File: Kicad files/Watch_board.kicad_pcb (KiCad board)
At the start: 2 copper layers, 45.5 x 35 mm, 60 parts, among them J1 USB_C_Receptacle_USB2.0, J2 MOT1, J3 MOT2, Q1 BC846, SW2 BTN_L, SW3 BTN_R, U1 LTC3531, U2 MAX1811, U3 BMP280, U4 DS3231MZ, U5 STM32L031K6Tx, U6 xc9141

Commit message: updated PCB version
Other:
- board text added: "STM32Watch v1.1"
- board text removed: "STM32Watch v1.0"
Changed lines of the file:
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@@
     (effects (font (size 1 1) (thickness 0.15)) (justify mirror))
   )
-  (gr_text "STM32Watch v1.0" (at 92 61.75 90) (layer "F.SilkS")
+  (gr_text "STM32Watch v1.1" (at 92 61.75 90) (layer "F.SilkS")
     (effects (font (size 1 1) (thickness 0.15)))
   )

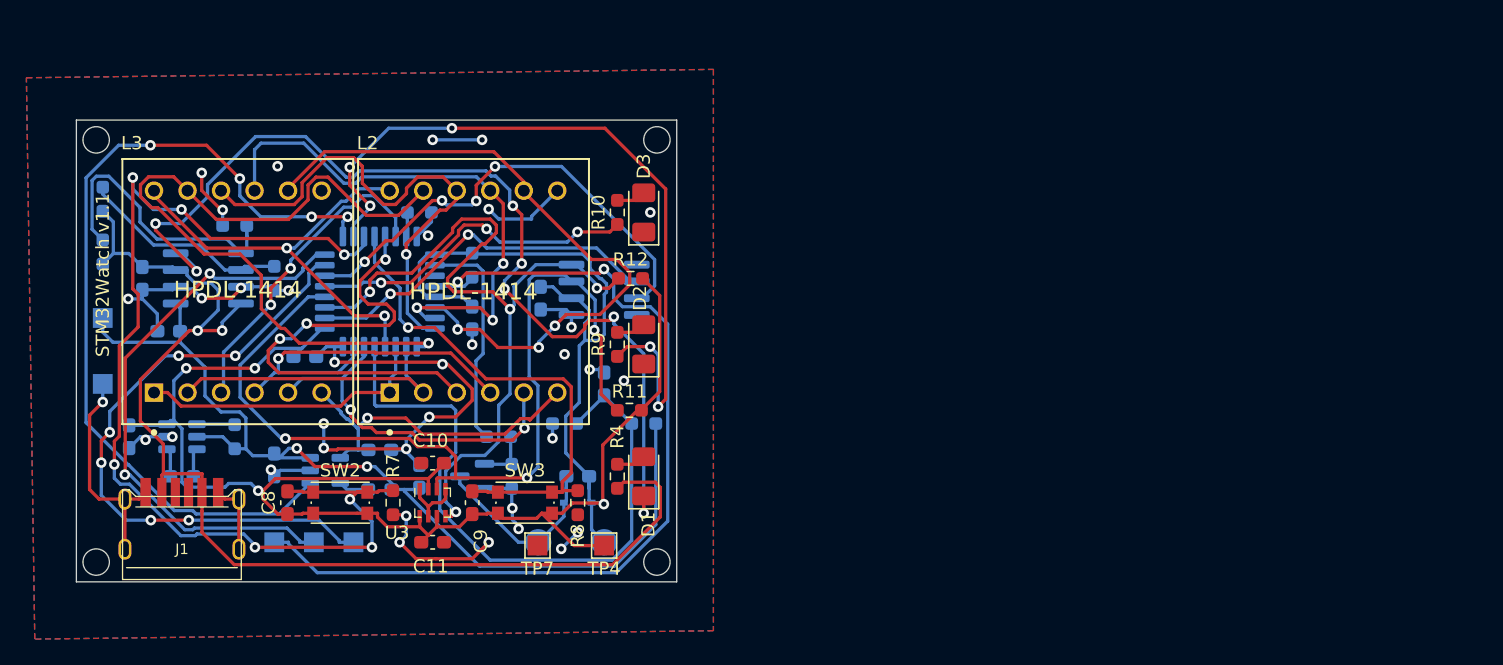
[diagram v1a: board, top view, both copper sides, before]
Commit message: updated to HCMS-2904 (WIP)
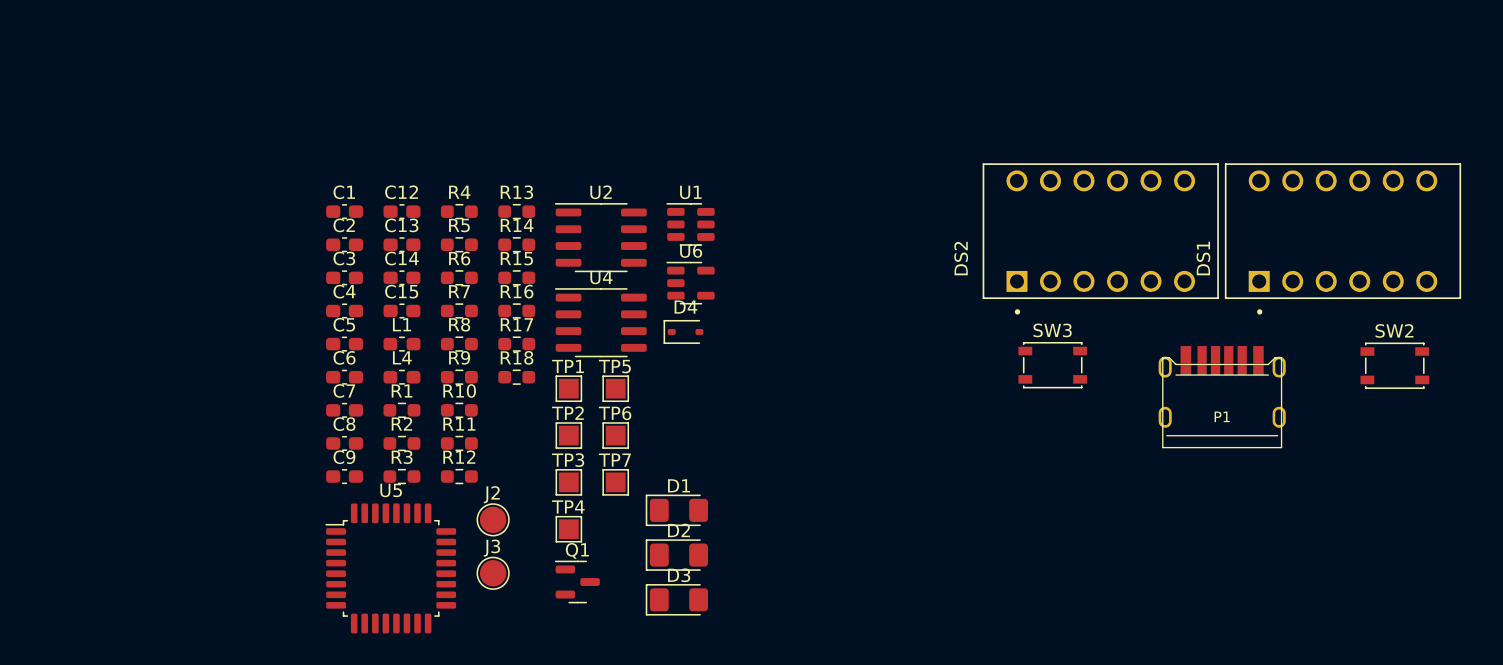
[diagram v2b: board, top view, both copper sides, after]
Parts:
- removed C10, C11: 0.1uF, Capacitor_SMD:C_0603_1608Metric_Pad1.08x0.95mm_HandSolder
- removed J1: USB_C_Receptacle_USB2.0, USB-C-Connectors:TYPE-C-31-M-17_handsolder
- removed L2, L3: HPDL-1414, eec:Broadcom-HPDL-1414-0
- removed U3: BMP280, Package_LGA:Bosch_LGA-8_2x2.5mm_P0.65mm_ClockwisePinNumbering
- added DS1: HCMS-2904, HCMS-290x:DIPS762W51P254L1778H508Q12, F.Cu at (186.0, 58.4)
- added DS2: HCMS-2904, HCMS-290x:DIPS762W51P254L1778H508Q12, F.Cu at (167.6, 58.4)
- added P1: USB_C_Plug_USB2.0, USB-C-Connectors:TYPE-C-31-M-17_handsolder, F.Cu at (176.8, 72.5)
- C1, C12, C13, C14, C15, C2, C3, C4, C5, C6, C7, D4, J2, J3, L1, L4, Q1, R1, R13, R14, R15, R16, R17, R18, R2, R3, R5, R6, TP1, TP2, TP3, TP5, TP6, U1, U2, U4, U5, U6: moved to F.Cu
- SW2, SW3: footprint Button_Switch_SMD:SW_Push_1P1T_NO_CK_KMR2 -> Button_Switch_SMD:SW_SPST_PTS810
- moved SW2 80.6 mm to (189.9, 68.6)
- moved U1 41.8 mm to (136.6, 57.9)
- moved SW3 41.3 mm to (164.0, 68.6)
- moved TP5 39.2 mm to (130.9, 70.4), turned to 0 degrees
- moved TP6 39.1 mm to (130.9, 73.9), turned to 0 degrees
- moved U6 31.1 mm to (136.6, 62.4)
- moved U2 29.9 mm to (129.8, 58.9), turned to 0 degrees
- moved D3 29.5 mm to (135.7, 86.4), turned to 0 degrees
- moved R6 27.7 mm to (119.0, 62.0), turned to 0 degrees
- moved R5 27.0 mm to (119.0, 59.5), turned to 0 degrees
- moved TP2 23.7 mm to (127.3, 73.9), turned to 0 degrees
- moved R4 23.4 mm to (119.0, 56.9), turned to 0 degrees
- moved R3 22.9 mm to (114.7, 77.0)
- moved C2 21.9 mm to (110.3, 59.5), turned to 0 degrees
- moved U5 21.0 mm to (113.9, 84.0), turned to 0 degrees
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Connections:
- U5 pad 21: LED_R -> unconnected-(U5-PA11-Pad21)
- U5 pad 26: LED_G -> unconnected-(U5-PB3-Pad26)
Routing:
- net 3V3: track 158.0 -> 0.00 mm, vias 4 -> 0
- net GND: track 127.3 -> 0.00 mm, vias 35 -> 0
- net VUSB: track 87.9 -> 0.00 mm, vias 2 -> 0
- net BTN_L: track 81.0 -> 0.00 mm, vias 7 -> 0
- net Net-(D1-K): track 75.5 -> 0.00 mm, vias 7 -> 0
- net BAT+: track 74.0 -> 0.00 mm, vias 2 -> 0
- net NRST: track 69.9 -> 0.00 mm, vias 2 -> 0
- net SDA: track 69.2 -> 0.00 mm, vias 3 -> 0
- net DISP_EN: track 64.9 -> 0.00 mm, vias 4 -> 0
- net SCL: track 59.7 -> 0.00 mm, vias 4 -> 0
- net LED_G: track 57.8 -> 0.00 mm, vias 5 -> 0
- net D3: track 56.8 -> 0.00 mm, vias 1 -> 0
- net D0: track 51.0 -> 0.00 mm, vias 3 -> 0
- net ADC: track 50.3 -> 0.00 mm
- net Net-(U5-PA13): track 48.7 -> 0.00 mm, vias 6 -> 0
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- removed copper zone on B.Cu, net GND
- removed copper zone on F.Cu, net GND
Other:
- board outline removed
- board text removed: "BAT+"
- board text removed: "BAT-"
- board text removed: "MOT1"
- board text removed: "MOT2"
- board text removed: "RES"
- board text removed: "STM32Watch v1.1"
- board text removed: "TCK"
- board text removed: "TMS"

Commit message: updated kicad schematics to add light sensor, updated code
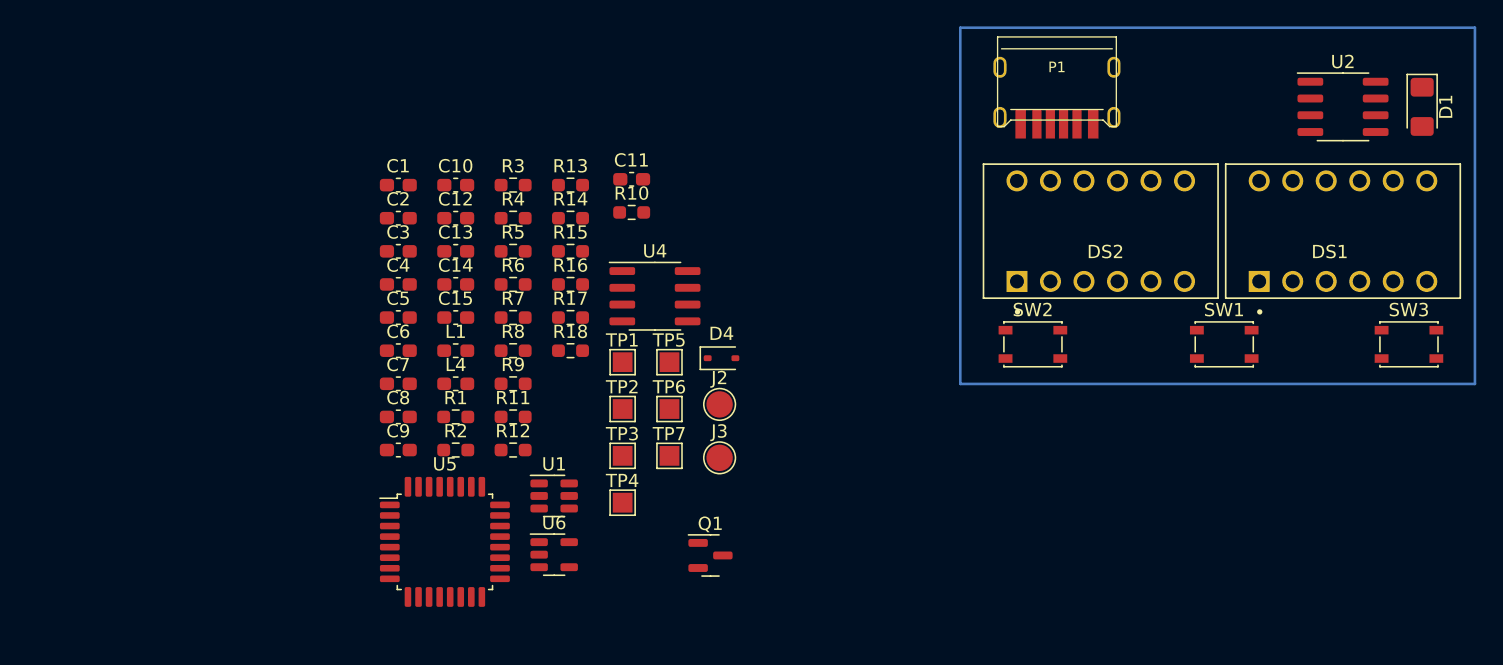
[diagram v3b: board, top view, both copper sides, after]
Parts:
- removed D2: LED_G, LED_SMD:LED_1206_3216Metric_Pad1.42x1.75mm_HandSolder
- removed D3: LED_R, LED_SMD:LED_1206_3216Metric_Pad1.42x1.75mm_HandSolder
- added C10: 0.1uF, Capacitor_SMD:C_0603_1608Metric_Pad1.08x0.95mm_HandSolder, F.Cu at (118.8, 54.9)
- added C11: 0.1uF, Capacitor_SMD:C_0603_1608Metric_Pad1.08x0.95mm_HandSolder, F.Cu at (132.1, 54.5)
- added SW1: BTN_M, Button_Switch_SMD:SW_SPST_PTS810, F.Cu at (177.0, 67.0)
- R10: value 4.7k -> 1k
- R9: value 22k -> 10k
- moved D1 64.1 mm to (192.0, 49.0), turned to -90 degrees
- moved U2 57.1 mm to (186.0, 49.0)
- moved P1 29.3 mm to (164.3, 46.0), turned to 180 degrees
- moved SW2 27.5 mm to (162.5, 67.0)
- moved SW3 27.0 mm to (191.0, 67.0)
- moved R3 23.6 mm to (123.1, 54.9)
- moved U1 23.0 mm to (126.2, 78.5)
- moved U6 23.0 mm to (126.2, 82.9)
- moved R10 19.9 mm to (132.1, 57.0)
- moved J2 19.3 mm to (138.8, 71.5)
- moved J3 19.3 mm to (138.8, 75.6)
- moved Q1 10.3 mm to (138.1, 83.0)
- moved C2 4.54 mm to (114.4, 57.4)
- moved C5 4.54 mm to (114.4, 65.0)
- moved C7 4.54 mm to (114.4, 70.0)
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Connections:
- R10 pad 1: LED_R -> 3V3
- R9 pad 1: LED_G -> GND
- R9 pad 2: Net-(D2-A) -> BTN_M
- U5 pad 26: unconnected-(U5-PB3-Pad26) -> BTN_M
